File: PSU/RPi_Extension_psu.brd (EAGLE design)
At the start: 63 x 50 mm, 40 parts, among them U1 ADP2303ARDZ-5.0, U2 TPS54356-EP_PWP_16, X1 MKDSN1,5/3-5,08

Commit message: updated pcbs
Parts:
- C1, C11, C14, C2, C7: value (none) -> 10uF
- C10, C13, C15, C3, C4: value (none) -> 0.1uF
- C12: value (none) -> 1.0uF
- C16: value (none) -> 1500pF
- C22: value (none) -> 220uF
- C23, C24: value (none) -> 100nF
- L1: value (none) -> 4.7uH
- L2: value (none) -> 22uH
- R1: value (none) -> 100k
- R2: value (none) -> 56k
- R3: value (none) -> 10.2k
- R4: value (none) -> 52.3k
- R5: value (none) -> 10k
- R6: value (none) -> 4.7
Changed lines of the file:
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@@
 </element>
 <element name="X1" library="con-phoenix-508" package="MKDSN1,5/3-5,08" value="MKDSN1,5/3-5,08" x="49.4" y="3.9" rot="R180"/>
-<element name="C1" library="rcl" package="C1206" value="" x="34.45" y="6.65" rot="MR90"/>
-<element name="C2" library="rcl" package="C1206" value="" x="31.6" y="9.55" rot="MR270"/>
-<element name="C3" library="rcl" package="C0603" value="" x="25.35" y="7.8" rot="MR270"/>
-<element name="C4" library="rcl" package="C0603" value="" x="22.75" y="8.45" rot="MR90"/>
+<element name="C1" library="rcl" package="C1206" value="10uF" x="34.45" y="6.65" rot="MR90"/>
+<element name="C2" library="rcl" package="C1206" value="10uF" x="31.6" y="9.55" rot="MR270"/>
+<element name="C3" library="rcl" package="C0603" value="0.1uF" x="25.35" y="7.8" rot="MR270"/>
+<element name="C4" library="rcl" package="C0603" value="0.1uF" x="22.75" y="8.45" rot="MR90"/>
 <element name="U1" library="ADP2303ARDZ" package="SOIC127P600X175-9N" value="ADP2303ARDZ-5.0" x="52.65" y="27.95" rot="R180">
 <attribute name="SUPPLIER" value="Analog Devices" x="52.65" y="27.95" size="1.778" layer="27" rot="R180" display="off"/>
@@
 <attribute name="OC_NEWARK" value="12T1264" x="52.65" y="27.95" size="1.778" layer="27" rot="R180" display="off"/>
 </element>
-<element name="C7" library="rcl" package="C0603" value="" x="58.65" y="24.65"/>
+<element name="C7" library="rcl" package="C0603" value="10uF" x="58.65" y="24.65"/>
 <element name="C8" library="rcl" package="C0603" value="" x="32.5" y="35.5" rot="R90"/>
 <element name="C9" library="rcl" package="C0603" value="" x="34.95" y="35.5" rot="R90"/>
-<element name="C10" library="rcl" package="C0603" value="" x="52.65" y="24.05" rot="R180"/>
-<element name="R1" library="rcl" package="R0603" value="" x="60.45" y="27.95" rot="R90"/>
-<element name="R2" library="rcl" package="R0603" value="" x="57.8" y="27.9" rot="R90"/>
-<element name="R3" library="rcl" package="R0603" value="" x="57.8" y="31.35" rot="R90"/>
-<element name="R4" library="rcl" package="R0603" value="" x="30.05" y="35.5" rot="R270"/>
-<element name="R5" library="rcl" package="R0603" value="" x="30.05" y="28.35" rot="R270"/>
+<element name="C10" library="rcl" package="C0603" value="0.1uF" x="52.65" y="24.05" rot="R180"/>
+<element name="R1" library="rcl" package="R0603" value="100k" x="60.45" y="27.95" rot="R90"/>
+<element name="R2" library="rcl" package="R0603" value="56k" x="57.8" y="27.9" rot="R90"/>
+<element name="R3" library="rcl" package="R0603" value="10.2k" x="57.8" y="31.35" rot="R90"/>
+<element name="R4" library="rcl" package="R0603" value="52.3k" x="30.05" y="35.5" rot="R270"/>
+<element name="R5" library="rcl" package="R0603" value="10k" x="30.05" y="28.35" rot="R270"/>
 <element name="D1" library="1smb59xx_10" package="DO214AA" value="1SMB5913BT3G" x="47.15" y="21.95" rot="R270">
 <attribute name="MPN" value="1SMB5913BT3G" x="47.15" y="21.95" size="1.778" layer="27" rot="R270" display="off"/>
@@
 <attribute name="OC_NEWARK" value="88H5165" x="47.15" y="21.95" size="1.778" layer="27" rot="R270" display="off"/>
 </element>
-<element name="L1" library="WE-PD" package="WE-PD_1030/1050" value="" x="42.25" y="31.85" rot="R90">
+<element name="L1" library="WE-PD" package="WE-PD_1030/1050" value="4.7uH" x="42.25" y="31.85" rot="R90">
 <attribute name="SUPPLIER" value="Wuerth Elektronik" x="42.25" y="31.85" size="1.778" layer="27" rot="R90" display="off"/>
 <attribute name="MPN" value="7447713047" x="42.25" y="31.85" size="1.778" layer="27" rot="R90" display="off"/>
@@
 <attribute name="INDUSTRY_STD_PKG_TYPE" value="HTSSOP" x="29.75" y="16.65" size="1.778" layer="27" rot="R180" display="off"/>
 </element>
-<element name="C11" library="rcl" package="C0603" value="" x="35.85" y="14.2" rot="R270"/>
-<element name="C12" library="rcl" package="C0603" value="" x="23.7" y="17.8" rot="R90"/>
-<element name="C13" library="rcl" package="C0603" value="" x="24.2" y="14.35" rot="R180"/>
-<element name="C14" library="rcl" package="C0603" value="" x="6.5" y="30.55" rot="R90"/>
-<element name="C15" library="rcl" package="C0603" value="" x="3.9" y="30.55" smashed="yes" rot="R90">
+<element name="C11" library="rcl" package="C0603" value="10uF" x="35.85" y="14.2" rot="R270"/>
+<element name="C12" library="rcl" package="C0603" value="1.0uF" x="23.7" y="17.8" rot="R90"/>
+<element name="C13" library="rcl" package="C0603" value="0.1uF" x="24.2" y="14.35" rot="R180"/>
+<element name="C14" library="rcl" package="C0603" value="10uF" x="6.5" y="30.55" rot="R90"/>
+<element name="C15" library="rcl" package="C0603" value="0.1uF" x="3.9" y="30.55" smashed="yes" rot="R90">
 <attribute name="NAME" x="3.265" y="29.915" size="1.27" layer="25" rot="R90"/>
 <attribute name="VALUE" x="5.805" y="29.915" size="1.27" layer="27" rot="R90"/>
 </element>
-<element name="C16" library="rcl" package="C0603" value="" x="26.65" y="7.15" rot="R270"/>
-<element name="R6" library="rcl" package="R0603" value="" x="26.65" y="10.4" rot="R270"/>
+<element name="C16" library="rcl" package="C0603" value="1500pF" x="26.65" y="7.15" rot="R270"/>
+<element name="R6" library="rcl" package="R0603" value="4.7" x="26.65" y="10.4" rot="R270"/>
 <element name="C17" library="Panasonic-EEEFK_EEEFP" package="CAPAE660X800N" value="100UF" x="40.15" y="21.5">
 <attribute name="SUPPLIER" value="PANASONIC" x="40.15" y="21.5" size="1.778" layer="27" display="off"/>
@@
 <attribute name="OC_NEWARK" value="45J2421" x="23.85" y="9.25" size="1.778" layer="27" rot="R270" display="off"/>
 </element>
-<element name="L2" library="WE-PD" package="WE-PD_1260/1245/1280/1210" value="" x="15.35" y="14.35" rot="R180">
+<element name="L2" library="WE-PD" package="WE-PD_1260/1245/1280/1210" value="22uH" x="15.35" y="14.35" rot="R180">
 <attribute name="SUPPLIER" value="Wuerth Elektronik" x="15.35" y="14.35" size="1.778" layer="27" rot="R180" display="off"/>
 <attribute name="MPN" value="744770122" x="15.35" y="14.35" size="1.778" layer="27" rot="R180" display="off"/>
@@
 <element name="C20" library="rcl" package="C0603" value="" x="28.6" y="46.8" rot="R270"/>
 <element name="C21" library="rcl" package="C0603" value="" x="31.15" y="46.8" rot="R270"/>
-<element name="C23" library="rcl" package="C0603" value="" x="12.35" y="36.4" rot="R90"/>
-<element name="C24" library="rcl" package="C0603" value="" x="16.25" y="36.4" rot="R90"/>
-<element name="C22" library="resistor" package="C1206" value="" x="24.45" y="35" rot="R270"/>
+<element name="C23" library="rcl" package="C0603" value="100nF" x="12.35" y="36.4" rot="R90"/>
+<element name="C24" library="rcl" package="C0603" value="100nF" x="16.25" y="36.4" rot="R90"/>
+<element name="C22" library="resistor" package="C1206" value="220uF" x="24.45" y="35" rot="R270"/>
 <element name="C25" library="Panasonic-EEEFT_EEEH" package="CAPAE830X1050N" value="680UF" x="55.65" y="12.85">
 <attribute name="OC_FARNELL" value="2065973  " x="55.65" y="12.85" size="1.778" layer="27" display="off"/>

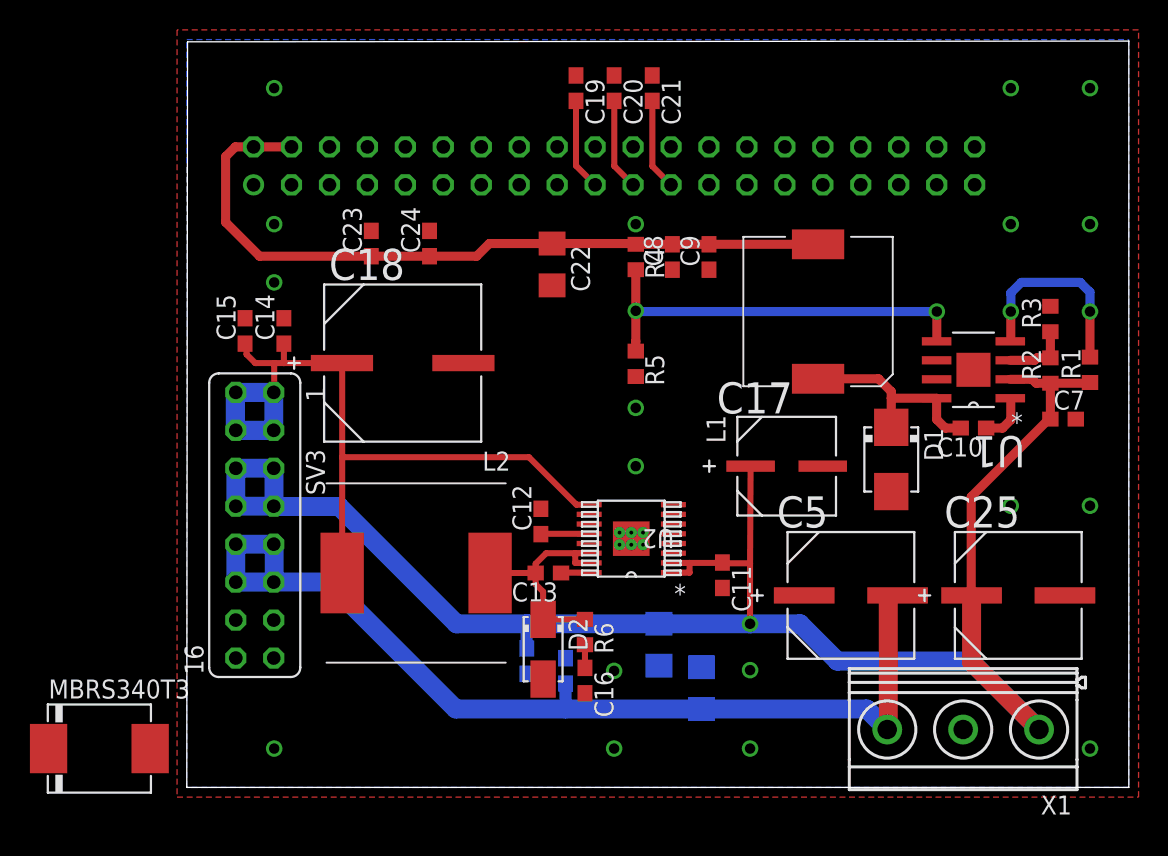
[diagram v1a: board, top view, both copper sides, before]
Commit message: reworked PSU layout
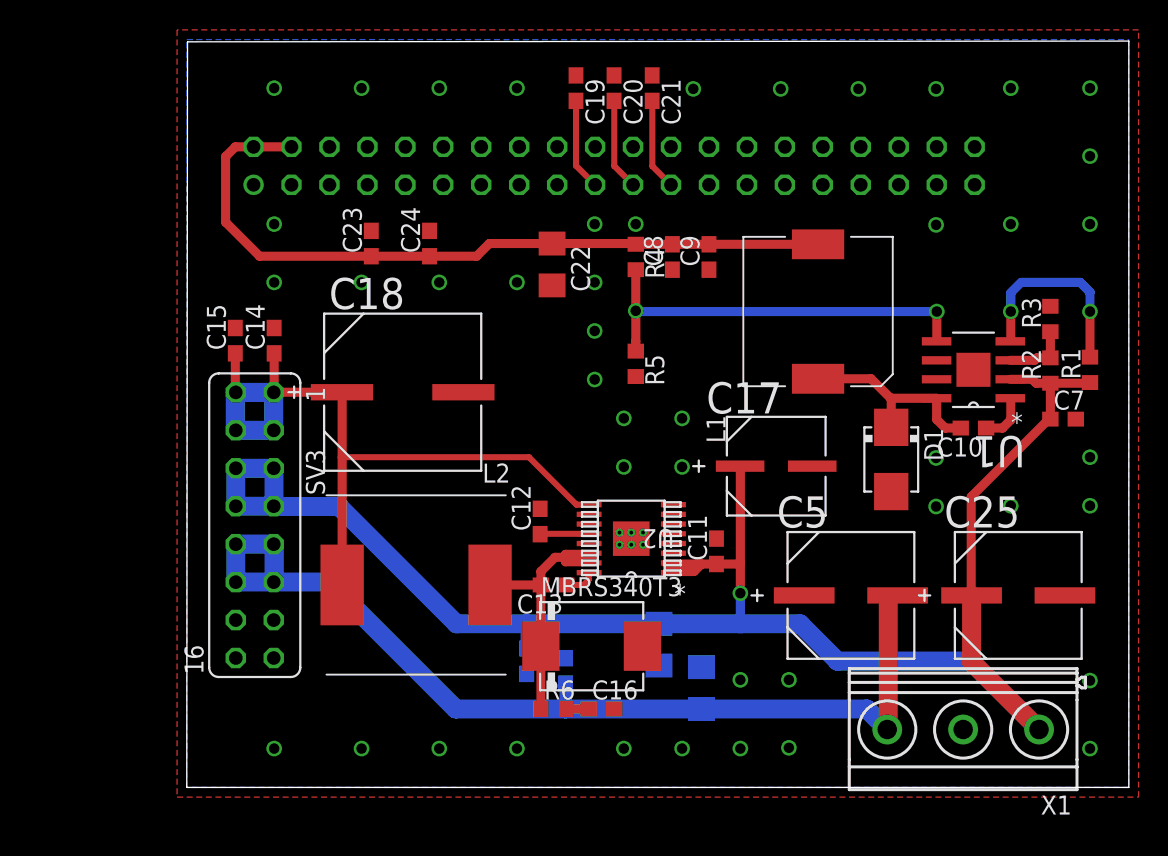
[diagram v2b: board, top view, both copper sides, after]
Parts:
- removed D2: 1SMA5934BT3G, 1sma59xx_10:DO214AC
- C10, C13, C15, C3, C4: value 0.1uF -> 100nF
- C17: value 100UF -> 100uF
- C18: value 330UF -> 330uF
- C25, C5: value 680UF -> 680uF
- C8: value (none) -> 47uF
- C9: value (none) -> 100nF
- moved MBRS340T3 33.7 mm to (27.1, 9.45)
- moved R6 5.56 mm to (24.6, 5.25), turned to 0 degrees
- moved C16 2.20 mm to (27.8, 5.25), turned to 0 degrees
- moved C18 1.95 mm to (14.4, 26.4)
- moved C11 1.65 mm to (35.5, 15.8), turned to 90 degrees
- moved C14 0.92 mm to (5.85, 29.9)
- moved C15 0.92 mm to (3.25, 29.9)
- moved C13 0.87 mm to (24.6, 13.6)
- moved L2 0.80 mm to (15.3, 13.6)
- moved C17 0.70 mm to (39.5, 21.5)
- moved C12 0.05 mm to (23.6, 17.8)
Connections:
- removed net N$10: C13.2, D2.C, L2.1, R6.1, U2.14, U2.15
- new net VOUT: C13.2, L2.1, MBRS340T3.C, R6.1, U2.14, U2.15
- net GND: now also MBRS340T3.A, U1.9; no longer D2.A
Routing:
- net VOUT: track 0.00 -> 19.9 mm
- net N$10: track 15.2 -> 0.00 mm
- net DVCC: track 55.2 -> 53.1 mm
- net VDD: track 119.6 -> 121.0 mm

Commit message: added additional id jumpers to adc and dac board
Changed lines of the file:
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@@
 <contactref element="C4" pad="2"/>
 <wire x1="31.6" y1="10.95" x2="22.75" y2="10.95" width="1.27" layer="16"/>
-<wire x1="22.75" y1="10.95" x2="18.05" y2="10.95" width="1.27" layer="16"/>
-<wire x1="18.05" y1="10.95" x2="10.2" y2="18.8" width="1.27" layer="16"/>
-<wire x1="10.2" y1="18.8" x2="5.84" y2="18.8" width="1.27" layer="16"/>
+<wire x1="22.75" y1="10.95" x2="20.75" y2="10.95" width="1.27" layer="16"/>
+<wire x1="12.9" y1="18.8" x2="5.84" y2="18.8" width="1.27" layer="16"/>
 <wire x1="5.84" y1="18.8" x2="5.82" y2="18.82" width="1.27" layer="16"/>
 <contactref element="U1" pad="2"/>
@@
 <wire x1="3.28" y1="21.36" x2="5.82" y2="21.36" width="1.27" layer="16"/>
 <wire x1="5.84" y1="18.78" x2="5.84" y2="21.32" width="1.27" layer="16"/>
-<wire x1="41.05" y1="10.95" x2="37.05" y2="10.95" width="1.27" layer="16"/>
 <wire x1="37.05" y1="10.95" x2="31.6" y2="10.95" width="1.27" layer="16"/>
-<wire x1="41.05" y1="10.95" x2="43.55" y2="8.45" width="1.27" layer="16"/>
 <contactref element="C25" pad="1"/>
-<wire x1="43.55" y1="8.45" x2="52.4661" y2="8.45" width="1.27" layer="16"/>
-<wire x1="52.4661" y1="8.45" x2="57.0411" y2="3.875" width="1.27" layer="16"/>
+<wire x1="49.9661" y1="10.95" x2="57.0411" y2="3.875" width="1.27" layer="16"/>
 <wire x1="57.8" y1="24.65" x2="57.7" y2="24.65" width="0.6096" layer="1"/>
 <wire x1="57.7" y1="24.65" x2="52.5" y2="19.45" width="0.6096" layer="1"/>
@@
 <wire x1="37.05" y1="15" x2="37.05" y2="21.487" width="0.6096" layer="1"/>
 <wire x1="37.05" y1="21.487" x2="37.037" y2="21.5" width="0.6096" layer="1"/>
+<wire x1="37.05" y1="10.95" x2="49.9661" y2="10.95" width="1.27" layer="16"/>
+<wire x1="12.9" y1="18.8" x2="20.75" y2="10.95" width="1.27" layer="16"/>
 <wire x1="5.84" y1="18.8" x2="5.84" y2="18.78" width="0" layer="19" extent="16-16"/>
 </signal>

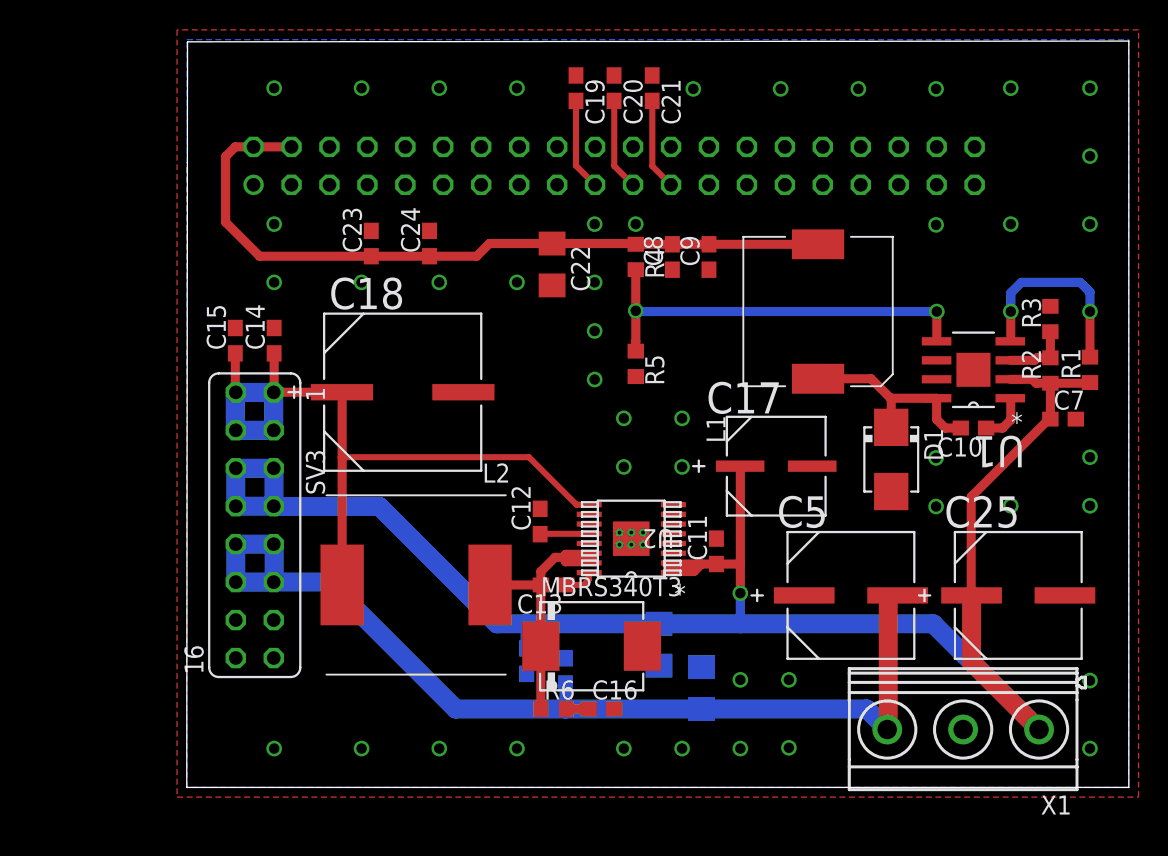
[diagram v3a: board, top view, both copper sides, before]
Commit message: cleaned up silklayer of psu board
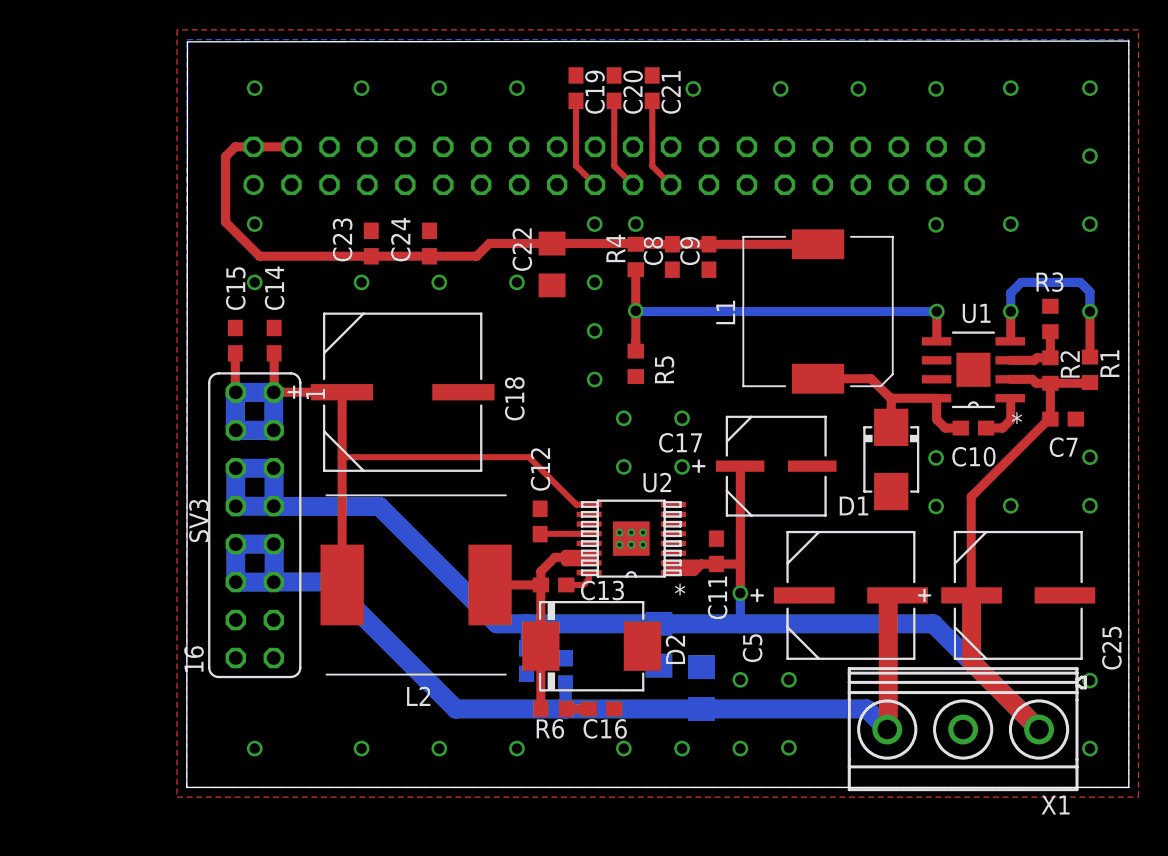
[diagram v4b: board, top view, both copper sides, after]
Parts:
- renumbered MBRS340T3 to D2
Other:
- board text added: "Hitzmann 2017"

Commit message: added more documentation
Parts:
- C8: value 47uF -> 22uF
- C9: value 100nF -> 22uF
- X1: value MKDSN1,5/3-5,08 -> (none)
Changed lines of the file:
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@@
 <attribute name="OC_NEWARK" value="unknown" x="28.6" y="41.6" size="1.778" layer="28" rot="MR180" display="off"/>
 </element>
-<element name="X1" library="con-phoenix-508" package="MKDSN1,5/3-5,08" value="MKDSN1,5/3-5,08" x="49.4" y="3.9" rot="R180"/>
+<element name="X1" library="con-phoenix-508" package="MKDSN1,5/3-5,08" value="" x="49.4" y="3.9" smashed="yes" rot="R180">
+<attribute name="NAME" x="43.6311" y="2.055" size="1.27" layer="25" rot="R180"/>
+<attribute name="VALUE" x="53.21" y="-0.545" size="1.27" layer="27" rot="R180"/>
+</element>
 <element name="C1" library="rcl" package="C1206" value="10uF" x="34.45" y="6.65" smashed="yes" rot="MR90">
 <attribute name="NAME" x="35.72" y="7.98" size="1.27" layer="26" rot="MR90"/>
@@
 <attribute name="VALUE" x="58.015" y="22.745" size="1.27" layer="27"/>
 </element>
-<element name="C8" library="rcl" package="C0603" value="47uF" x="32.5" y="35.5" rot="R90"/>
-<element name="C9" library="rcl" package="C0603" value="100nF" x="34.95" y="35.5" rot="R90"/>
+<element name="C8" library="rcl" package="C0603" value="22uF" x="32.5" y="35.5" rot="R90"/>
+<element name="C9" library="rcl" package="C0603" value="22uF" x="34.95" y="35.5" rot="R90"/>
 <element name="C10" library="rcl" package="C0603" value="100nF" x="52.65" y="24.05" smashed="yes" rot="R180">
 <attribute name="NAME" x="54.235" y="22.765" size="1.27" layer="25" rot="R180"/>
@@
 <attribute name="TOLERANCE" value="±20 %" x="44.45" y="12.85" size="1.778" layer="27" display="off"/>
 <attribute name="VOLTAGERATING" value="16V" x="44.45" y="12.85" size="1.778" layer="27" display="off"/>
-<attribute name="NAME" x="38.5034" y="8.297" size="1.27" layer="25" ratio="10" rot="SR90"/>
+<attribute name="NAME" x="38.7534" y="8.297" size="1.27" layer="25" ratio="10" rot="SR90"/>
 <attribute name="VALUE" x="38.9128" y="6.2206" size="2.0828" layer="27" ratio="10" rot="SR0"/>
 </element>
